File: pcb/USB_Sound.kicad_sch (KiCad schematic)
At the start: 34 parts, among them IC1 PCM2706, J1 USB4500-03-0-A_REVA, J2 Conn_Coaxial_x2, U5 FSUSB42MUX, U6 24AA02-OT, Y1 Crystal

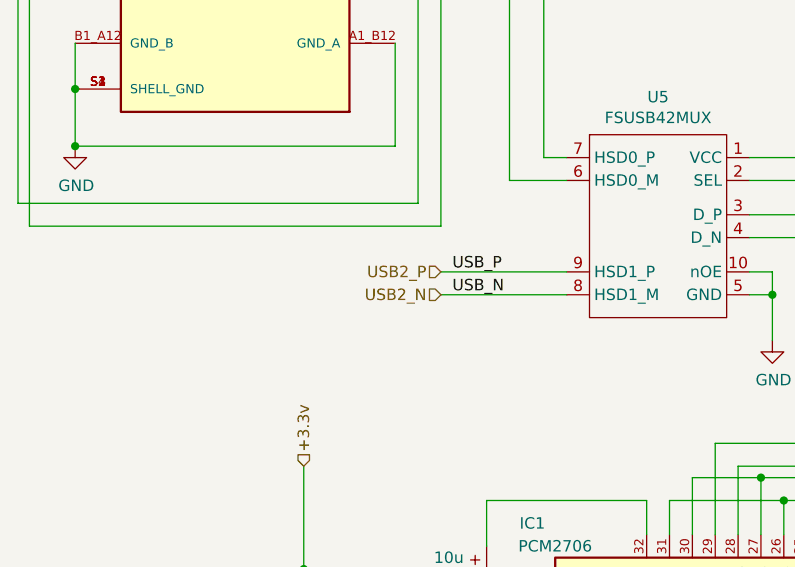
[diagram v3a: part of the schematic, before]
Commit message: - voor aanpassing design rules jclpcb
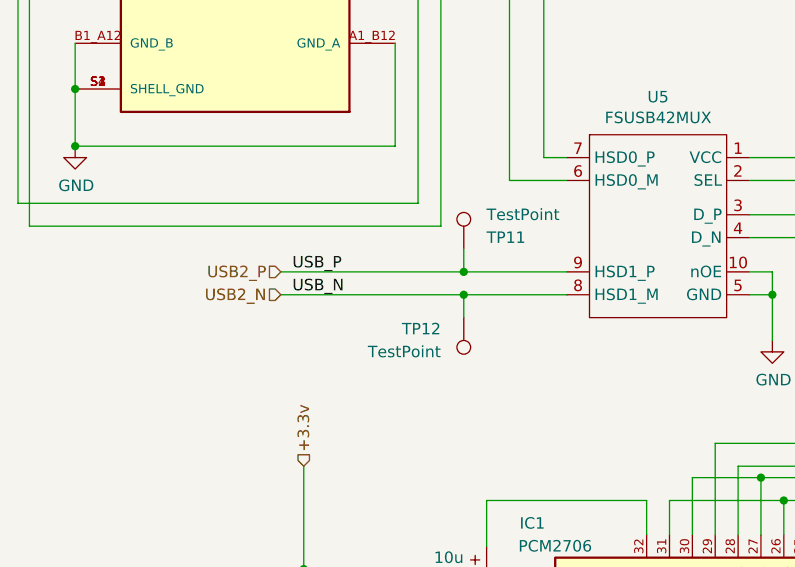
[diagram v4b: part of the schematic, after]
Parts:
- added TP11, TP12: TestPoint, TestPoint:TestPoint_Bridge_Pitch2.54mm_Drill1.0mm, symbol Connector:TestPoint
- C4, C5, C6, C7: footprint (none) -> Capacitor_SMD:C_0805_2012Metric_Pad1.18x1.45mm_HandSolder
- R10, R11, R12, R13, R14, R15, R16, R6, R7, R9: footprint (none) -> Resistor_SMD:R_0805_2012Metric_Pad1.20x1.40mm_HandSolder
- R8: footprint Resistor_SMD:R_0402_1005Metric -> Resistor_SMD:R_0805_2012Metric_Pad1.20x1.40mm_HandSolder
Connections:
- net USB2_N: now also TP12.1
- net USB2_P: now also TP11.1
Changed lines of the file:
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@@
   (junction (at 151.13 102.87) (diameter 0) (color 0 0 0 0)
   )
+  (junction (at 68.58 81.28) (diameter 0) (color 0 0 0 0)
+  )
   (junction (at 135.89 102.87) (diameter 0) (color 0 0 0 0)
   )
@@
   )
   (junction (at 25.4 67.31) (diameter 0) (color 0 0 0 0)
+  )
+  (junction (at 68.58 83.82) (diameter 0) (color 0 0 0 0)
   )
   (junction (at 151.13 185.42) (diameter 0) (color 0 0 0 0)
@@
     (stroke (width 0) (type default))
   )
+  (wire (pts (xy 48.26 83.82) (xy 68.58 83.82))
+    (stroke (width 0) (type default))
+  )
   (wire (pts (xy 119.38 123.19) (xy 120.65 123.19))
     (stroke (width 0) (type default))
   )
-  (wire (pts (xy 66.04 83.82) (xy 80.01 83.82))
-    (stroke (width 0) (type default))
-  )
   (wire (pts (xy 156.21 100.33) (xy 156.21 105.41))
     (stroke (width 0) (type default))
@@
     (stroke (width 0) (type default))
   )
+  (wire (pts (xy 68.58 83.82) (xy 80.01 83.82))
+    (stroke (width 0) (type default))
+  )
   (wire (pts (xy 102.87 81.28) (xy 102.87 83.82))
     (stroke (width 0) (type default))
@@
     (stroke (width 0) (type default))
   )
+  (wire (pts (xy 68.58 81.28) (xy 80.01 81.28))
+    (stroke (width 0) (type default))
+  )
   (wire (pts (xy 101.6 177.8) (xy 116.84 177.8))
     (stroke (width 0) (type default))
@@
     (stroke (width 0) (type default))
   )
-  (wire (pts (xy 66.04 81.28) (xy 80.01 81.28))
+  (wire (pts (xy 48.26 81.28) (xy 68.58 81.28))
     (stroke (width 0) (type default))
   )
@@
     (stroke (width 0) (type default))
   )
+  (wire (pts (xy 68.58 78.74) (xy 68.58 81.28))
+    (stroke (width 0) (type default))
+  )
   (wire (pts (xy 50.8 114.3) (xy 50.8 123.19))
     (stroke (width 0) (type default))
@@
   )
   (wire (pts (xy 88.9 153.67) (xy 88.9 163.83))
+    (stroke (width 0) (type default))
+  )
+  (wire (pts (xy 68.58 83.82) (xy 68.58 86.36))
     (stroke (width 0) (type default))
   )
@@
     (effects (font (size 1.27 1.27)) (justify left bottom))
   )
-  (label "USB_P" (at 67.31 81.28 0) (fields_autoplaced)
+  (label "USB_P" (at 49.53 81.28 0) (fields_autoplaced)
     (effects (font (size 1.27 1.27)) (justify left bottom))
   )
@@
     (effects (font (size 1.27 1.27)) (justify left bottom))
   )
-  (label "USB_N" (at 67.31 83.82 0) (fields_autoplaced)
+  (label "USB_N" (at 49.53 83.82 0) (fields_autoplaced)
     (effects (font (size 1.27 1.27)) (justify left bottom))
   )
@@
     (effects (font (size 1.27 1.27)) (justify left bottom))
   )
-  (hierarchical_label "USB2_P" (shape input) (at 66.04 81.28 180) (fields_autoplaced)
+  (hierarchical_label "USB2_P" (shape input) (at 48.26 81.28 180) (fields_autoplaced)
     (effects (font (size 1.27 1.27)) (justify right))
   )
@@
     (effects (font (size 1.27 1.27)) (justify left))
   )
-  (hierarchical_label "USB2_N" (shape input) (at 66.04 83.82 180) (fields_autoplaced)
+  (hierarchical_label "USB2_N" (shape input) (at 48.26 83.82 180) (fields_autoplaced)
     (effects (font (size 1.27 1.27)) (justify right))
   )
@@
       (effects (font (size 1.27 1.27)) (justify left))
     )
-    (property "Footprint" "" (at 149.352 109.22 90)
+    (property "Footprint" "Resistor_SMD:R_0805_2012Metric_Pad1.20x1.40mm_HandSolder" (at 149.352 109.22 90)
       (effects (font (size 1.27 1.27)) hide)
     )
@@
       (effects (font (size 1.27 1.27)) (justify left))
     )
-    (property "Footprint" "" (at 154.432 109.22 90)
+    (property "Footprint" "Resistor_SMD:R_0805_2012Metric_Pad1.20x1.40mm_HandSolder" (at 154.432 109.22 90)
       (effects (font (size 1.27 1.27)) hide)
     )
@@
       (effects (font (size 1.27 1.27)) (justify left))
     )
-    (property "Footprint" "" (at 181.102 109.22 90)
+    (property "Footprint" "Resistor_SMD:R_0805_2012Metric_Pad1.20x1.40mm_HandSolder" (at 181.102 109.22 90)
       (effects (font (size 1.27 1.27)) hide)
     )
@@
       (effects (font (size 1.27 1.27)) (justify left))
     )
-    (property "Footprint" "" (at 105.1052 190.5 0)
+    (property "Footprint" "Capacitor_SMD:C_0805_2012Metric_Pad1.18x1.45mm_HandSolder" (at 105.1052 190.5 0)
       (effects (font (size 1.27 1.27)) hide)
     )
@@
       (effects (font (size 1.27 1.27)) (justify left))
     )
-    (property "Footprint" "" (at 134.112 118.11 90)
+    (property "Footprint" "Resistor_SMD:R_0805_2012Metric_Pad1.20x1.40mm_HandSolder" (at 134.112 118.11 90)
       (effects (font (size 1.27 1.27)) hide)
     )
@@
       (effects (font (size 1.27 1.27)))
     )
-    (property "Footprint" "" (at 96.52 175.768 90)
+    (property "Footprint" "Resistor_SMD:R_0805_2012Metric_Pad1.20x1.40mm_HandSolder" (at 96.52 175.768 90)
       (effects (font (size 1.27 1.27)) hide)
     )
@@
       (effects (font (size 1.27 1.27)) (justify left))
     )
-    (property "Footprint" "" (at 134.112 167.64 90)
+    (property "Footprint" "Resistor_SMD:R_0805_2012Metric_Pad1.20x1.40mm_HandSolder" (at 134.112 167.64 90)
       (effects (font (size 1.27 1.27)) hide)
     )
@@
       (effects (font (size 1.27 1.27)) (justify left))
     )
-    (property "Footprint" "" (at 136.8552 113.03 0)
+    (property "Footprint" "Capacitor_SMD:C_0805_2012Metric_Pad1.18x1.45mm_HandSolder" (at 136.8552 113.03 0)
       (effects (font (size 1.27 1.27)) hide)
     )
@@
       (effects (font (size 1.27 1.27)) (justify left))
     )
-    (property "Footprint" "" (at 88.5952 190.5 0)
+    (property "Footprint" "Capacitor_SMD:C_0805_2012Metric_Pad1.18x1.45mm_HandSolder" (at 88.5952 190.5 0)
       (effects (font (size 1.27 1.27)) hide)
     )
@@
       (effects (font (size 1.27 1.27)) (justify left))
     )
-    (property "Footprint" "" (at 143.2052 113.03 0)
+    (property "Footprint" "Capacitor_SMD:C_0805_2012Metric_Pad1.18x1.45mm_HandSolder" (at 143.2052 113.03 0)
       (effects (font (size 1.27 1.27)) hide)
     )
@@
       (effects (font (size 1.27 1.27)) (justify left))
     )
-    (property "Footprint" "" (at 140.462 118.11 90)
+    (property "Footprint" "Resistor_SMD:R_0805_2012Metric_Pad1.20x1.40mm_HandSolder" (at 140.462 118.11 90)
       (effects (font (size 1.27 1.27)) hide)
     )
@@
       (effects (font (size 1.27 1.27)) (justify left))
     )
-    (property "Footprint" "" (at 130.302 167.64 90)
+    (property "Footprint" "Resistor_SMD:R_0805_2012Metric_Pad1.20x1.40mm_HandSolder" (at 130.302 167.64 90)
       (effects (font (size 1.27 1.27)) hide)
     )
@@
       (effects (font (size 1.27 1.27)) (justify left))
     )
-    (property "Footprint" "" (at 174.752 109.22 90)
+    (property "Footprint" "Resistor_SMD:R_0805_2012Metric_Pad1.20x1.40mm_HandSolder" (at 174.752 109.22 90)
       (effects (font (size 1.27 1.27)) hide)
     )
@@
       (effects (font (size 1.27 1.27)) (justify left))
     )
-    (property "Footprint" "Resistor_SMD:R_0402_1005Metric" (at 103.632 46.99 90)
+    (property "Footprint" "Resistor_SMD:R_0805_2012Metric_Pad1.20x1.40mm_HandSolder" (at 103.632 46.99 90)
       (effects (font (size 1.27 1.27)) hide)
     )
@@
     )
   )
+  (symbol (lib_id "Connector:TestPoint") (at 68.58 86.36 180) (unit 1)
+    (in_bom yes) (on_board yes) (dnp no)
+    (property "Reference" "TP12" (at 66.04 87.63 0)
+      (effects (font (size 1.27 1.27)) (justify left))
+    )
+    (property "Value" "TestPoint" (at 66.04 90.17 0)
+      (effects (font (size 1.27 1.27)) (justify left))
+    )
+    (property "Footprint" "TestPoint:TestPoint_Bridge_Pitch2.54mm_Drill1.0mm" (at 63.5 86.36 0)
+      (effects (font (size 1.27 1.27)) hide)
+    )
+    (property "Datasheet" "~" (at 63.5 86.36 0)
+      (effects (font (size 1.27 1.27)) hide)
+    )
+    (pin "1")
+    (instances
+      (project "VolumioAmp"
+        (path "/c639bae0-d26f-43ee-9e8c-ca060284bd0b/93301fd2-7a6d-48be-bd24-243a1877e343"
+          (reference "TP12") (unit 1)
+        )
+      )
+    )
+  )
   (symbol (lib_id "Connector:Conn_Coaxial_x2") (at 201.93 100.33 0) (unit 1)
     (in_bom yes) (on_board yes) (dnp no) (fields_autoplaced)
@@
     )
   )
+  (symbol (lib_id "Connector:TestPoint") (at 68.58 78.74 0) (unit 1)
+    (in_bom yes) (on_board yes) (dnp no)
+    (property "Reference" "TP11" (at 71.12 77.47 0)
+      (effects (font (size 1.27 1.27)) (justify left))
+    )
+    (property "Value" "TestPoint" (at 71.12 74.93 0)
+      (effects (font (size 1.27 1.27)) (justify left))
+    )
+    (property "Footprint" "TestPoint:TestPoint_Bridge_Pitch2.54mm_Drill1.0mm" (at 73.66 78.74 0)
+      (effects (font (size 1.27 1.27)) hide)
+    )
+    (property "Datasheet" "~" (at 73.66 78.74 0)
+      (effects (font (size 1.27 1.27)) hide)
+    )
+    (pin "1")
+    (instances
+      (project "VolumioAmp"
+        (path "/c639bae0-d26f-43ee-9e8c-ca060284bd0b/93301fd2-7a6d-48be-bd24-243a1877e343"
+          (reference "TP11") (unit 1)
+        )
+      )
+    )
+  )
   (symbol (lib_id "Device:R") (at 46.99 123.19 0) (unit 1)
     (in_bom yes) (on_board yes) (dnp no)
@@
       (effects (font (size 1.27 1.27)) (justify left))
     )
-    (property "Footprint" "" (at 45.212 123.19 90)
-      (effects (font (size 1.27 1.27)) hide)
-    )
+    (property "Footprint" "Resistor_SMD:R_0805_2012Metric_Pad1.20x1.40mm_HandSolder" (at 45.212 123.19 90)
+      (effects (font (size 1.27 1.27)) hide)
+    )

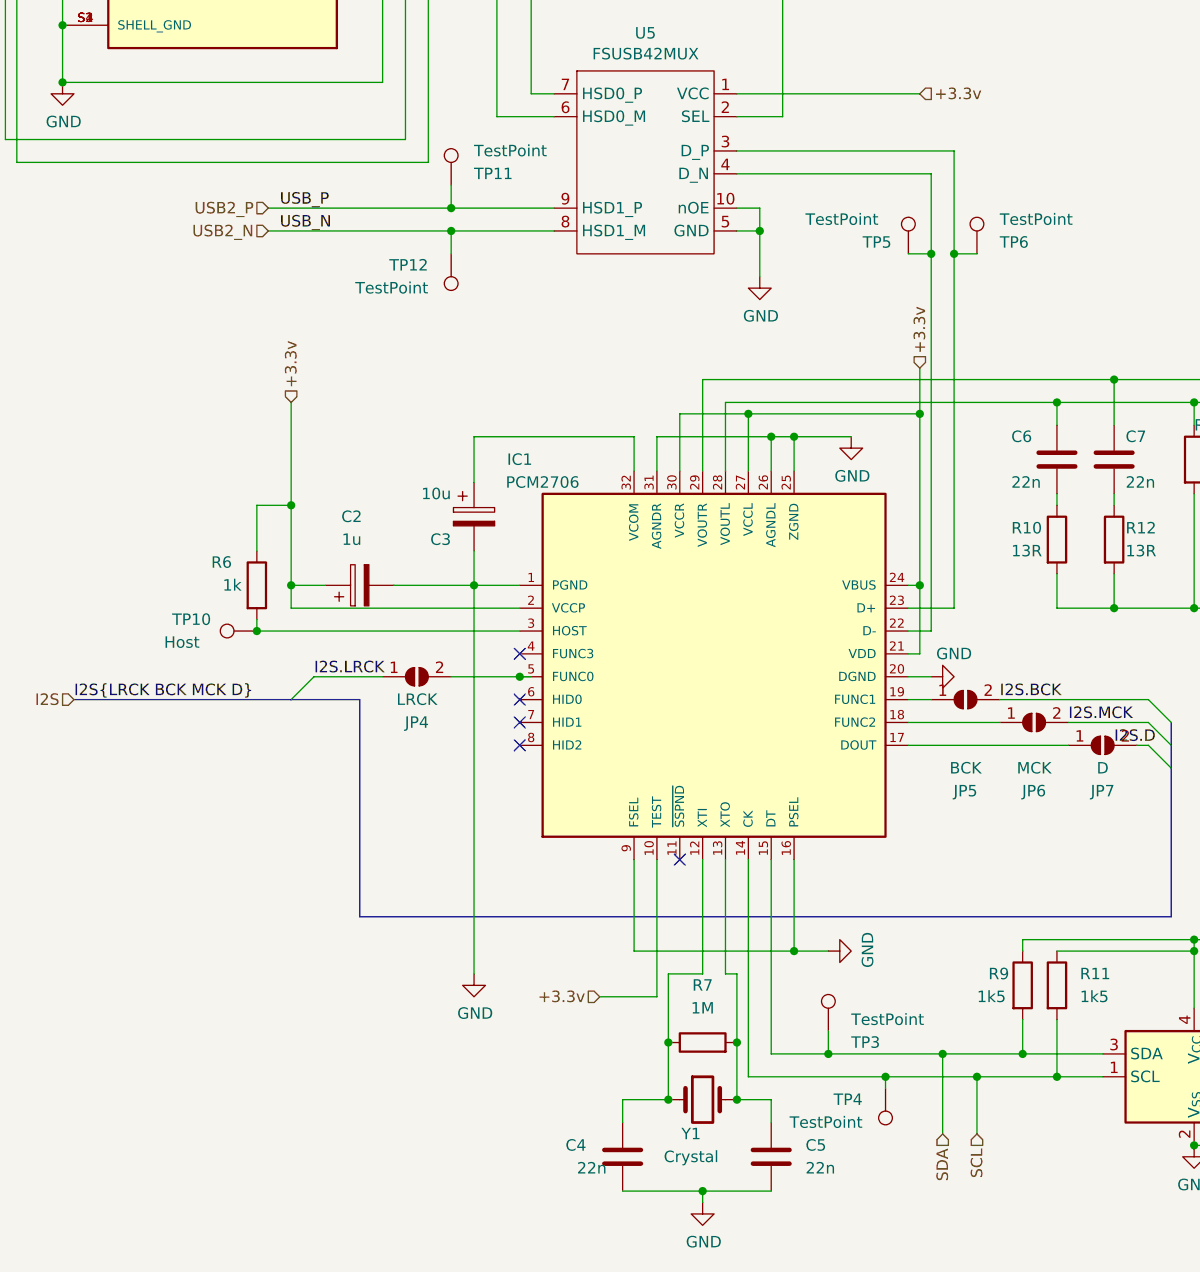
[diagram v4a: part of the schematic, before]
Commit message: - amp connected
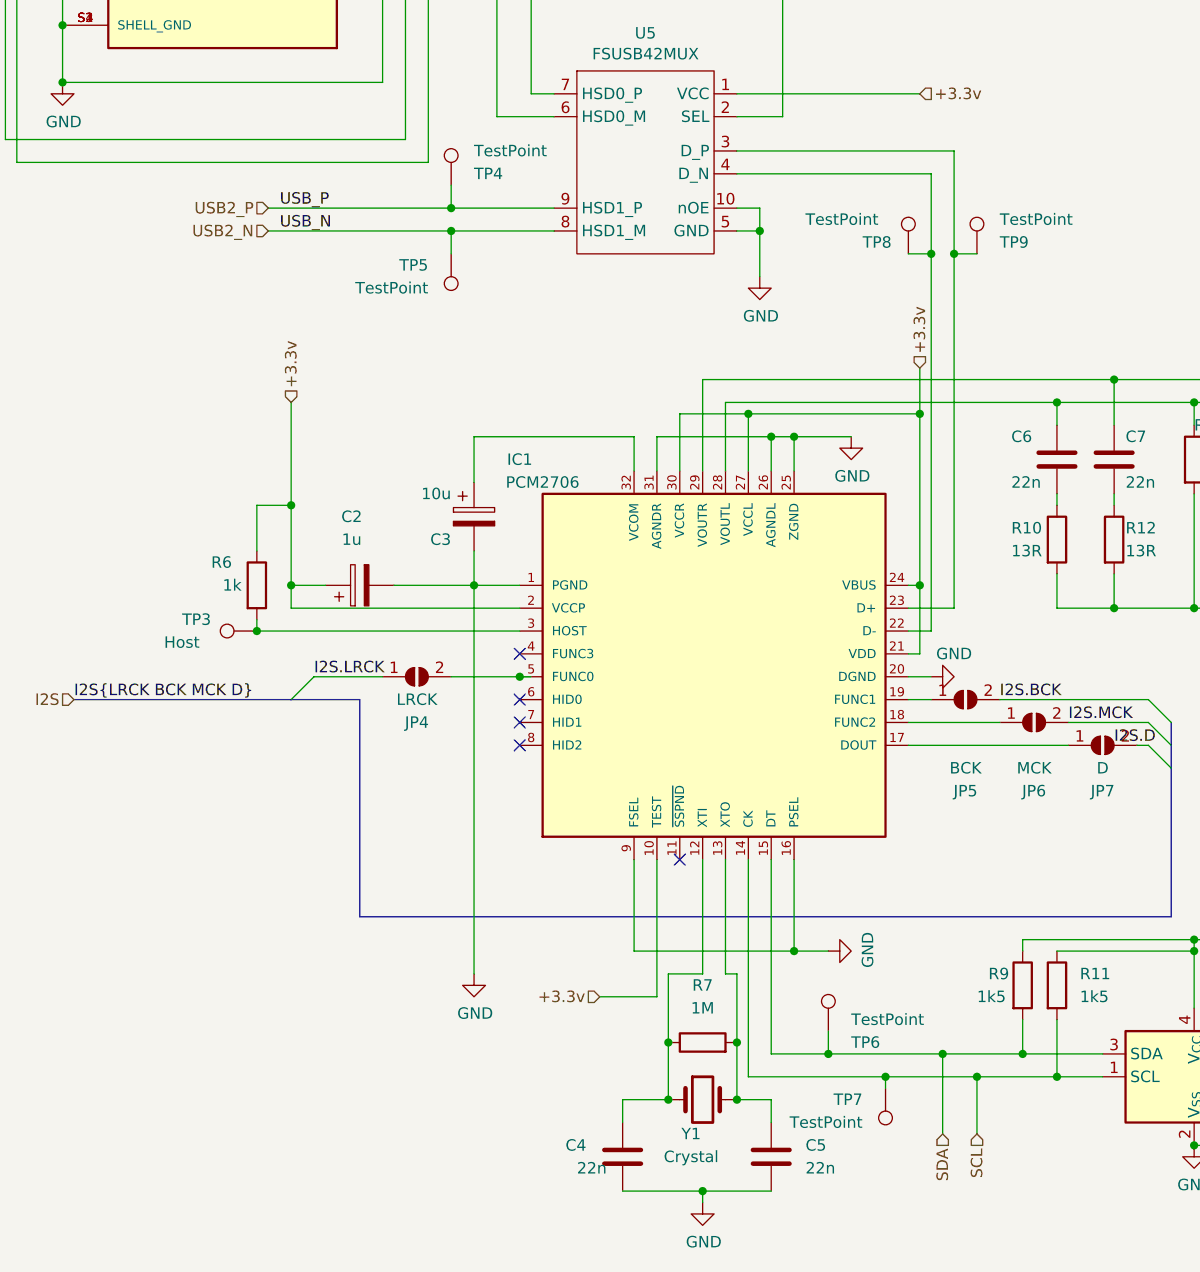
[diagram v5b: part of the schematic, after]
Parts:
- JP4, JP5, JP6, JP7: footprint (none) -> Jumper:SolderJumper-2_P1.3mm_Open_TrianglePad1.0x1.5mm
- renumbered TP10 to TP3, TP11 to TP4, TP12 to TP5, TP3 to TP6, TP4 to TP7, TP5 to TP8, TP6 to TP9
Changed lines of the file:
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@@
   (symbol (lib_id "Connector:TestPoint") (at 119.38 86.36 0) (unit 1)
     (in_bom yes) (on_board yes) (dnp no)
-    (property "Reference" "TP5" (at 114.3 85.09 0)
+    (property "Reference" "TP8" (at 114.3 85.09 0)
       (effects (font (size 1.27 1.27)) (justify left))
     )
@@
       (project "VolumioAmp"
         (path "/c639bae0-d26f-43ee-9e8c-ca060284bd0b/93301fd2-7a6d-48be-bd24-243a1877e343"
-          (reference "TP5") (unit 1)
+          (reference "TP8") (unit 1)
         )
       )
@@
   (symbol (lib_id "Connector:TestPoint") (at 46.99 128.27 90) (unit 1)
     (in_bom yes) (on_board yes) (dnp no)
-    (property "Reference" "TP10" (at 41.91 127 90)
+    (property "Reference" "TP3" (at 41.91 127 90)
       (effects (font (size 1.27 1.27)) (justify left))
     )
@@
       (project "VolumioAmp"
         (path "/c639bae0-d26f-43ee-9e8c-ca060284bd0b/93301fd2-7a6d-48be-bd24-243a1877e343"
-          (reference "TP10") (unit 1)
+          (reference "TP3") (unit 1)
         )
       )
@@
       (effects (font (size 1.27 1.27)))
     )
-    (property "Footprint" "" (at 125.73 135.89 0)
+    (property "Footprint" "Jumper:SolderJumper-2_P1.3mm_Open_TrianglePad1.0x1.5mm" (at 125.73 135.89 0)
       (effects (font (size 1.27 1.27)) hide)
     )
@@
       (effects (font (size 1.27 1.27)))
     )
-    (property "Footprint" "" (at 64.77 133.35 0)
+    (property "Footprint" "Jumper:SolderJumper-2_P1.3mm_Open_TrianglePad1.0x1.5mm" (at 64.77 133.35 0)
       (effects (font (size 1.27 1.27)) hide)
     )
@@
       (effects (font (size 1.27 1.27)))
     )
-    (property "Footprint" "" (at 133.35 138.43 0)
+    (property "Footprint" "Jumper:SolderJumper-2_P1.3mm_Open_TrianglePad1.0x1.5mm" (at 133.35 138.43 0)
       (effects (font (size 1.27 1.27)) hide)
     )
@@
   (symbol (lib_id "Connector:TestPoint") (at 127 86.36 0) (unit 1)
     (in_bom yes) (on_board yes) (dnp no)
-    (property "Reference" "TP6" (at 129.54 85.09 0)
+    (property "Reference" "TP9" (at 129.54 85.09 0)
       (effects (font (size 1.27 1.27)) (justify left))
     )
@@
       (project "VolumioAmp"
         (path "/c639bae0-d26f-43ee-9e8c-ca060284bd0b/93301fd2-7a6d-48be-bd24-243a1877e343"
-          (reference "TP6") (unit 1)
+          (reference "TP9") (unit 1)
         )
       )
@@
       (effects (font (size 1.27 1.27)))
     )
-    (property "Footprint" "" (at 140.97 140.97 0)
+    (property "Footprint" "Jumper:SolderJumper-2_P1.3mm_Open_TrianglePad1.0x1.5mm" (at 140.97 140.97 0)
       (effects (font (size 1.27 1.27)) hide)
     )
@@
   (symbol (lib_id "Connector:TestPoint") (at 110.49 172.72 0) (unit 1)
     (in_bom yes) (on_board yes) (dnp no)
-    (property "Reference" "TP3" (at 113.03 173.99 0)
+    (property "Reference" "TP6" (at 113.03 173.99 0)
       (effects (font (size 1.27 1.27)) (justify left))
     )
@@
       (project "VolumioAmp"
         (path "/c639bae0-d26f-43ee-9e8c-ca060284bd0b/93301fd2-7a6d-48be-bd24-243a1877e343"
-          (reference "TP3") (unit 1)
+          (reference "TP6") (unit 1)
         )
       )
@@
   (symbol (lib_id "Connector:TestPoint") (at 68.58 86.36 180) (unit 1)
     (in_bom yes) (on_board yes) (dnp no)
-    (property "Reference" "TP12" (at 66.04 87.63 0)
+    (property "Reference" "TP5" (at 66.04 87.63 0)
       (effects (font (size 1.27 1.27)) (justify left))
     )
@@
       (project "VolumioAmp"
         (path "/c639bae0-d26f-43ee-9e8c-ca060284bd0b/93301fd2-7a6d-48be-bd24-243a1877e343"
-          (reference "TP12") (unit 1)
+          (reference "TP5") (unit 1)
         )
       )
@@
   (symbol (lib_id "Connector:TestPoint") (at 68.58 78.74 0) (unit 1)
     (in_bom yes) (on_board yes) (dnp no)
-    (property "Reference" "TP11" (at 71.12 77.47 0)
+    (property "Reference" "TP4" (at 71.12 77.47 0)
       (effects (font (size 1.27 1.27)) (justify left))
     )
@@
       (project "VolumioAmp"
         (path "/c639bae0-d26f-43ee-9e8c-ca060284bd0b/93301fd2-7a6d-48be-bd24-243a1877e343"
-          (reference "TP11") (unit 1)
+          (reference "TP4") (unit 1)
         )
       )
@@
   (symbol (lib_id "Connector:TestPoint") (at 116.84 179.07 180) (unit 1)
     (in_bom yes) (on_board yes) (dnp no)
-    (property "Reference" "TP4" (at 114.3 180.34 0)
+    (property "Reference" "TP7" (at 114.3 180.34 0)
       (effects (font (size 1.27 1.27)) (justify left))
     )
@@
       (project "VolumioAmp"
         (path "/c639bae0-d26f-43ee-9e8c-ca060284bd0b/93301fd2-7a6d-48be-bd24-243a1877e343"
-          (reference "TP4") (unit 1)
-        )
-      )
+          (reference "TP7") (unit 1)
+        )
+      )
